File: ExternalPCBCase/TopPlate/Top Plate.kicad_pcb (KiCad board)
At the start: 2 copper layers, 150 x 104.9 mm, 9 parts

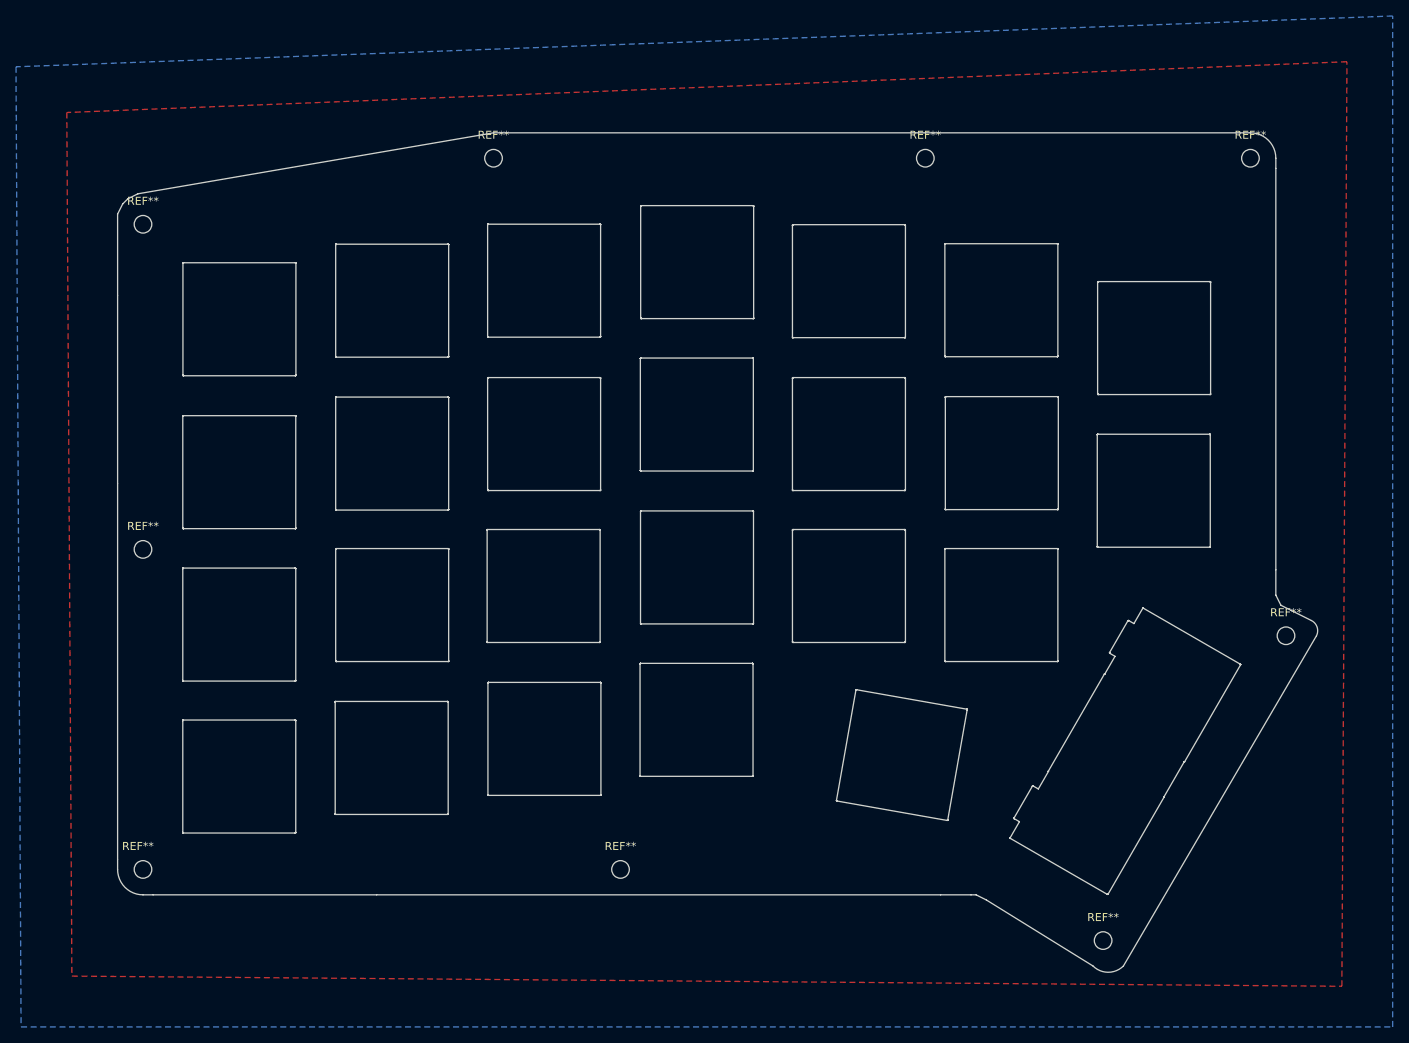
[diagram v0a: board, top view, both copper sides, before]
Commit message: Updating Internal Plates with Alps/MX Openings
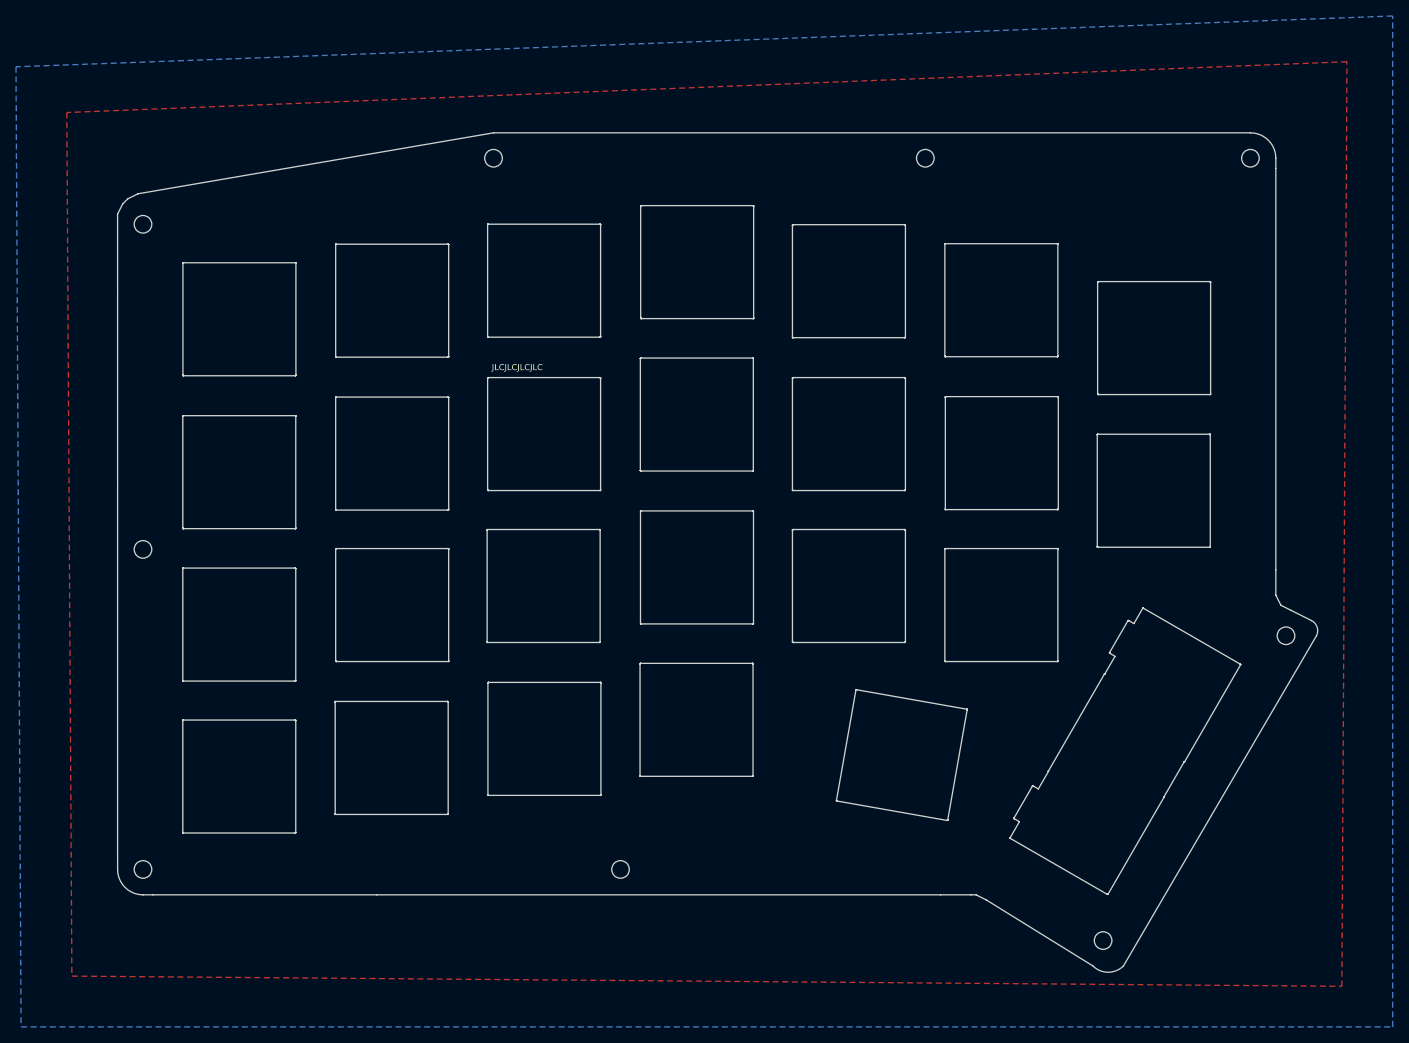
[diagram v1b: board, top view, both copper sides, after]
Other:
- board text added: "JLCJLCJLCJLC"
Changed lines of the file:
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@@
     (area 56.515 26.035 232.338572 152.400001)
     (thickness 1.6)
-    (drawings 2143)
+    (drawings 2144)
     (tracks 0)
     (zones 0)
@@
     (visible_elements 7FFFFFFF)
     (pcbplotparams
-      (layerselection 0x01000_00000000)
+      (layerselection 0x010f0_80000001)
       (usegerberextensions false)
       (excludeedgelayer true)
@@
       (padsonsilk false)
       (subtractmaskfromsilk false)
-      (outputformat 3)
+      (outputformat 1)
       (mirror false)
       (drillshape 0)
       (scaleselection 1)
-      (outputdirectory ./))
+      (outputdirectory Gerber/))
   )
   (net 0 "")
@@
     (tags "mounting hole 2.2mm no annular m2 din965")
     (attr virtual)
-    (fp_text reference REF** (at 0 -2.9) (layer F.SilkS)
+    (fp_text reference REF** (at 0 -2.9) (layer F.SilkS) hide
       (effects (font (size 1 1) (thickness 0.15)))
     )
@@
     (tags "mounting hole 2.2mm no annular m2 din965")
     (attr virtual)
-    (fp_text reference REF** (at 0 -2.9) (layer F.SilkS)
+    (fp_text reference REF** (at 0 -2.9) (layer F.SilkS) hide
       (effects (font (size 1 1) (thickness 0.15)))
     )
@@
     (tags "mounting hole 2.2mm no annular m2 din965")
     (attr virtual)
-    (fp_text reference REF** (at 0 -2.9) (layer F.SilkS)
+    (fp_text reference REF** (at 0 -2.9) (layer F.SilkS) hide
       (effects (font (size 1 1) (thickness 0.15)))
     )
@@
     (tags "mounting hole 2.2mm no annular m2 din965")
     (attr virtual)
-    (fp_text reference REF** (at -0.635 -2.9) (layer F.SilkS)
+    (fp_text reference REF** (at -0.635 -2.9) (layer F.SilkS) hide
       (effects (font (size 1 1) (thickness 0.15)))
     )
@@
     (tags "mounting hole 2.2mm no annular m2 din965")
     (attr virtual)
-    (fp_text reference REF** (at 0 -2.9) (layer F.SilkS)
+    (fp_text reference REF** (at 0 -2.9) (layer F.SilkS) hide
       (effects (font (size 1 1) (thickness 0.15)))
     )
@@
     (tags "mounting hole 2.2mm no annular m2 din965")
     (attr virtual)
-    (fp_text reference REF** (at 0 -2.9) (layer F.SilkS)
+    (fp_text reference REF** (at 0 -2.9) (layer F.SilkS) hide
       (effects (font (size 1 1) (thickness 0.15)))
     )
@@
     (tags "mounting hole 2.2mm no annular m2 din965")
     (attr virtual)
-    (fp_text reference REF** (at 0 -2.9) (layer F.SilkS)
+    (fp_text reference REF** (at 0 -2.9) (layer F.SilkS) hide
       (effects (font (size 1 1) (thickness 0.15)))
     )
@@
     (tags "mounting hole 2.2mm no annular m2 din965")
     (attr virtual)
-    (fp_text reference REF** (at 0 -2.9) (layer F.SilkS)
+    (fp_text reference REF** (at 0 -2.9) (layer F.SilkS) hide
       (effects (font (size 1 1) (thickness 0.15)))
     )
@@
     (tags "mounting hole 2.2mm no annular m2 din965")
     (attr virtual)
-    (fp_text reference REF** (at 0 -2.9) (layer F.SilkS)
+    (fp_text reference REF** (at 0 -2.9) (layer F.SilkS) hide
       (effects (font (size 1 1) (thickness 0.15)))
     )
@@
     (pad 1 np_thru_hole circle (at 0 0) (size 2.2 2.2) (drill 2.2) (layers *.Cu *.Mask))
   )
+  (gr_text JLCJLCJLCJLC (at 119.1768 69.9516) (layer F.SilkS)
+    (effects (font (size 0.75 0.75) (thickness 0.15)))
+  )
   (gr_line (start 214.63 99.695) (end 215.9 100.33) (layer Edge.Cuts) (width 0.15))
